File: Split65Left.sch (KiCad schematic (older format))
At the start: 69 parts, among them J1 Jack4, J2 OLED, SW1 SW_PUSH, SW10 SW_PUSH, SW11 SW_PUSH, SW12 SW_PUSH, SW13 SW_PUSH, SW14 SW_PUSH, SW15 SW_PUSH, SW16 SW_PUSH, SW17 SW_PUSH, SW18 SW_PUSH, SW19 SW_PUSH, SW2 SW_PUSH, SW20 SW_PUSH, SW21 SW_PUSH, SW22 SW_PUSH, SW23 SW_PUSH, SW24 SW_PUSH, SW25 SW_PUSH, SW26 SW_PUSH, SW27 SW_PUSH, SW28 SW_PUSH, SW29 SW_PUSH, SW3 SW_PUSH, SW30 SW_PUSH, SW31 SW_RST, SW4 SW_PUSH, SW5 SW_PUSH, SW6 SW_PUSH, SW7 SW_PUSH, SW8 SW_PUSH, SW9 SW_PUSH, U1 proton_c

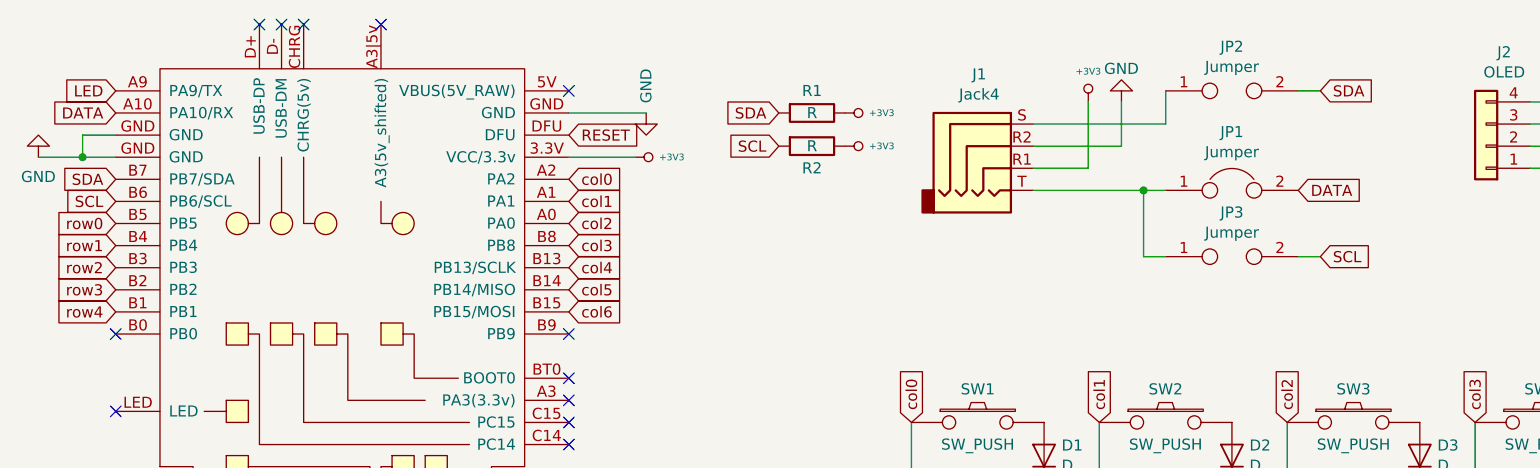
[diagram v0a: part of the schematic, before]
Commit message: modified:   Split65Left-cache.lib 	modified:   Split65Left.kicad_pcb 	modified:   Split65Left.kicad_pcb-bak 	modified:   Split65Left.net 	modified:   Split65Left.sch 	modified:   Split65Left.sch-bak 	modified:   Split65Right-cache.lib 	modified:   Split65Right.kicad_pcb 	modified:   Split65Right.kicad_pcb-bak 	modified:   Split65Right.net 	modified:   Split65Right.sch 	modified:   Split65Right.sch-bak
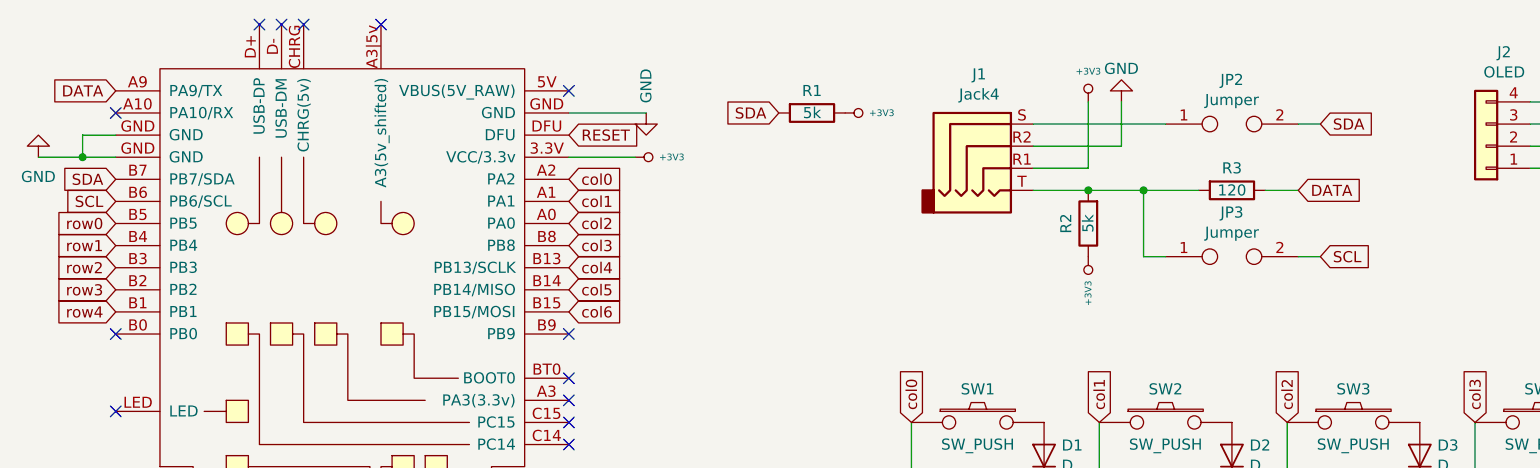
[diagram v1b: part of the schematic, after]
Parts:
- removed JP1: Jumper, footprints:jumper_data, symbol Device:Jumper
- added R3: 120, footprints:R_1608_axial, symbol Device:R
- R1, R2: value R -> 5k
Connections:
- net LED is gone; now on net DATA: U1.A9 (PA9/TX)
- net DATA: now also R3.1; no longer U1.A10 (PA10/RX)
- net SCL: no longer R2.2
- net at J1.T, JP3.1: now also R2.2, R3.2
- no-connect marks 24 -> 25
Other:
- moved on the sheet: JP2, R2
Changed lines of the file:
@@
 	1    0    0    -1
 $EndComp
-Text GLabel 1750 1600 0    50   Input ~ 0
+Text GLabel 1750 1500 0    50   Input ~ 0
 DATA
 Text GLabel 1750 1900 0    50   Input ~ 0
@@
 Text GLabel 1750 2000 0    50   Input ~ 0
 SCL
-Text GLabel 1750 1500 0    50   Input ~ 0
-LED
 Text GLabel 3800 1700 2    50   Input ~ 0
 RESET
@@
 	5900 1650 6500 1650
 Wire Wire Line
-	5900 1950 6400 1950
-$Comp
-L Device:Jumper JP1
-U 1 1 5F6D4F69
-P 6800 1950
-F 0 "JP1" H 6800 2214 50  0000 C CNN
-F 1 "Jumper" H 6800 2123 50  0000 C CNN
-F 2 "footprints:jumper_data" H 6800 1950 50  0001 C CNN
-F 3 "~" H 6800 1950 50  0001 C CNN
-	1    6800 1950
-	1    0    0    -1
-$EndComp
+	5900 1950 6150 1950
 Text GLabel 7100 1950 2    50   Input ~ 0
 DATA
 Text GLabel 4750 1600 0    50   Input ~ 0
 SDA
-Text GLabel 4750 1750 0    50   Input ~ 0
-SCL
 $Comp
 L Device:R R1
@@
 P 4900 1600
 F 0 "R1" V 4800 1600 50  0000 C CNN
-F 1 "R" V 4900 1600 50  0000 C CNN
+F 1 "5k" V 4900 1600 50  0000 C CNN
 F 2 "footprints:R_1608_axial" V 4830 1600 50  0001 C CNN
 F 3 "~" H 4900 1600 50  0001 C CNN
@@
 L Device:R R2
 U 1 1 5F6D7D30
-P 4900 1750
-F 0 "R2" V 5000 1750 50  0000 C CNN
-F 1 "R" V 4900 1750 50  0000 C CNN
-F 2 "footprints:R_1608_axial" V 4830 1750 50  0001 C CNN
-F 3 "~" H 4900 1750 50  0001 C CNN
-	1    4900 1750
-	0    1    1    0
+P 6150 2100
+F 0 "R2" V 6250 2100 50  0000 C CNN
+F 1 "5k" V 6150 2100 50  0000 C CNN
+F 2 "footprints:R_1608_axial" V 6080 2100 50  0001 C CNN
+F 3 "~" H 6150 2100 50  0001 C CNN
+	1    6150 2100
+	-1   0    0    1
 $EndComp
 $Comp
@@
 L keyboard_parts:+3V3 #PWR0107
 U 1 1 5F6D8E13
-P 5050 1750
-F 0 "#PWR0107" H 5050 1720 20  0001 C CNN
-F 1 "+3V3" V 5050 1858 30  0000 L CNN
-F 2 "" H 5050 1750 60  0000 C CNN
-F 3 "" H 5050 1750 60  0000 C CNN
-	1    5050 1750
-	0    1    1    0
-$EndComp
-Text GLabel 7200 1500 2    50   Input ~ 0
+P 6150 2250
+F 0 "#PWR0107" H 6150 2220 20  0001 C CNN
+F 1 "+3V3" V 6150 2358 30  0000 L CNN
+F 2 "" H 6150 2250 60  0000 C CNN
+F 3 "" H 6150 2250 60  0000 C CNN
+	1    6150 2250
+	-1   0    0    1
+$EndComp
+Text GLabel 7200 1650 2    50   Input ~ 0
 SDA
 Text GLabel 7200 2250 2    50   Input ~ 0
@@
 L keyboard_parts:Jumper JP2
 U 1 1 5F6F6359
-P 6800 1500
-F 0 "JP2" H 6800 1700 50  0000 C CNN
-F 1 "Jumper" H 6800 1609 50  0000 C CNN
-F 2 "footprints:Jumper" H 6800 1500 50  0001 C CNN
-F 3 "" H 6800 1500 50  0001 C CNN
-	1    6800 1500
+P 6800 1650
+F 0 "JP2" H 6800 1850 50  0000 C CNN
+F 1 "Jumper" H 6800 1759 50  0000 C CNN
+F 2 "footprints:Jumper" H 6800 1650 50  0001 C CNN
+F 3 "" H 6800 1650 50  0001 C CNN
+	1    6800 1650
 	1    0    0    -1
 $EndComp
@@
 $EndComp
 Wire Wire Line
-	7200 1500 7100 1500
-Wire Wire Line
-	6500 1500 6500 1650
+	7200 1650 7100 1650
 Wire Wire Line
 	6500 2250 6400 2250
@@
 	6400 2250 6400 1950
 Connection ~ 6400 1950
-Wire Wire Line
-	6400 1950 6500 1950
 Wire Wire Line
 	7100 2250 7200 2250
@@
 	0    1    1    0
 $EndComp
+NoConn ~ 1750 1600
+$Comp
+L Device:R R3
+U 1 1 5F7A3BBB
+P 6800 1950
+F 0 "R3" V 6700 1950 50  0000 C CNN
+F 1 "120" V 6800 1950 50  0000 C CNN
+F 2 "footprints:R_1608_axial" V 6730 1950 50  0001 C CNN
+F 3 "~" H 6800 1950 50  0001 C CNN
+	1    6800 1950
+	0    1    1    0
+$EndComp
+Connection ~ 6150 1950
+Wire Wire Line
+	6150 1950 6400 1950
+Wire Wire Line
+	7100 1950 6950 1950
+Wire Wire Line
+	6400 1950 6650 1950
 $EndSCHEMATC

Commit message: Updated some small things - removed 3u buttons
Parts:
- SW30: footprint footprints:KailhSocket-3U -> footprints:KailhSocket-2.75U
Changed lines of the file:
@@
 F 0 "SW30" H 9050 5150 50  0000 C CNN
 F 1 "SW_PUSH" H 9050 4900 50  0000 C CNN
-F 2 "footprints:KailhSocket-3U" H 9050 5000 60  0001 C CNN
+F 2 "footprints:KailhSocket-2.75U" H 9050 5000 60  0001 C CNN
 F 3 "" H 9050 5000 60  0000 C CNN
 	1    9050 5000
